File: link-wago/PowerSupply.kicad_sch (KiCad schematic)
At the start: 8 parts, among them U501 TPSM33625

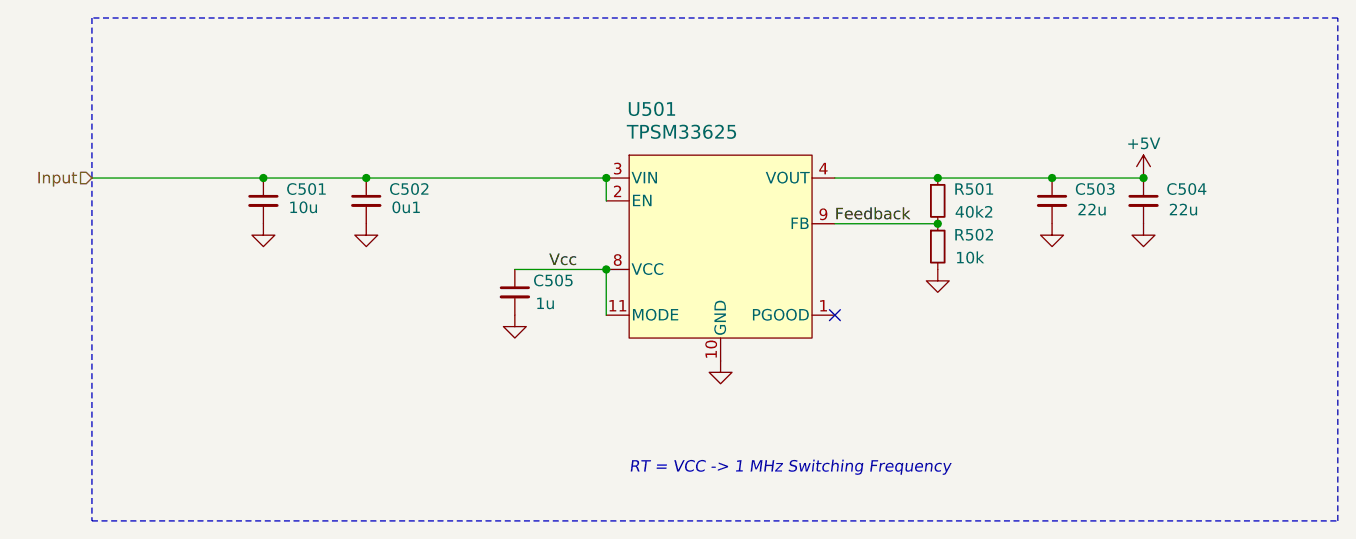
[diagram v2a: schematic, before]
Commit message: Replace step-down
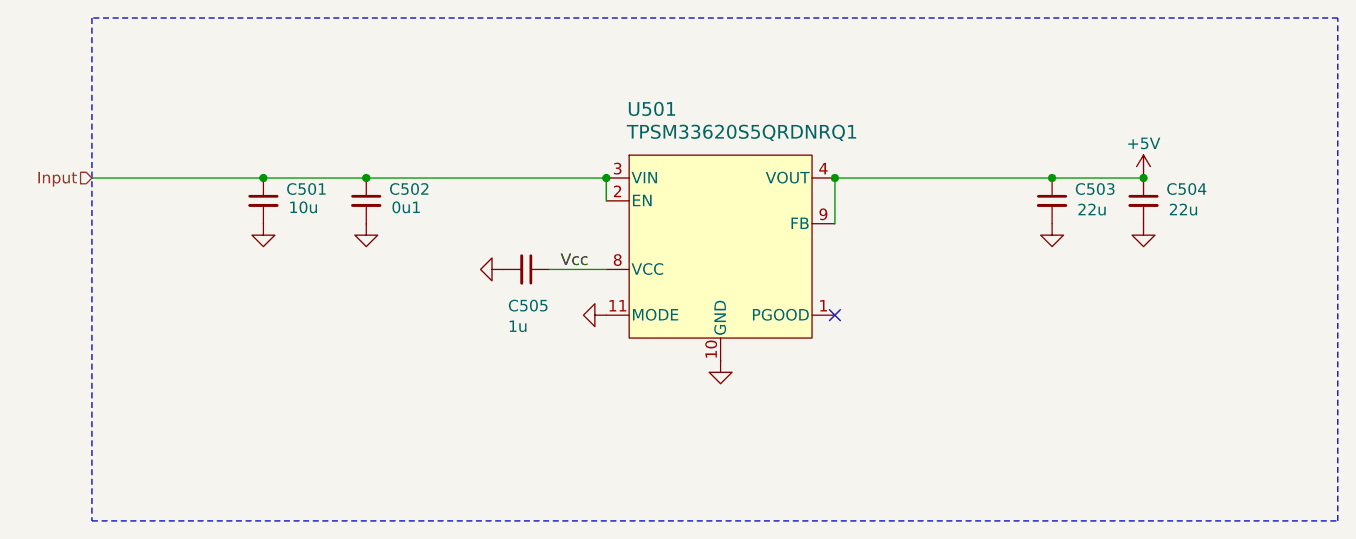
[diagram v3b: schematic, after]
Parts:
- removed R501: 40k2, V2_Resistor_SMD:R_0603, symbol V2_Resistor:0603_40k2
- removed R502: 10k, V2_Resistor_SMD:R_0603, symbol V2_Resistor:0603_10k
- U501: value TPSM33625 -> TPSM33620S5QRDNRQ1; symbol V2_Converter_DCDC:TPSM33625RDNR -> V2_Converter_DCDC:TPSM33620S5QRDNRQ1; Mouser 595-TPSM33625RDNR -> 595-SM33620S5QRDNRQ1; Product TPSM33625RDNR -> TPSM33620S5QRDNRQ1; Rating 2.5A -> 2A
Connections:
- net Feedback is gone; now on net +5V: U501.9 (FB)
- net GND: now also U501.11 (MODE)
- net Vcc: no longer U501.11 (MODE)
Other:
- note removed: "RT = VCC -> 1 MHz Switching Frequency"
- title: Power Supply -> V2 Link WAGO
- moved on the sheet: C505

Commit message: Update
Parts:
- C501: Id (none) -> Capacitor:${SYMBOL_NAME}; Mouser 810-CNA6P1X7R1H106K2 -> 810-CNC6P1X7R1H106K2; Product CNA6P1X7R1H106K250AE -> CNC6P1X7R1H106K250AE
- C502: Id (none) -> Capacitor:${SYMBOL_NAME}
- C503: renamed from C505; Id (none) -> Capacitor:${SYMBOL_NAME}
- C504: renamed from C503; Id (none) -> Capacitor:${SYMBOL_NAME}
- C505: renamed from C504; Id (none) -> Capacitor:${SYMBOL_NAME}
- U501: Id (none) -> DCDC:${SYMBOL_NAME}
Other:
- company: +5V -> Versio Duo
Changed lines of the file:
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@@
 	(title_block
 		(title "V2 Link WAGO")
-		(date "2026-03-31")
+		(date "2026-04-14")
 		(rev "2026-03-31")
-		(company "+5V")
+		(company "Versio Duo")
+		(comment 1 "External Power Supply")
 	)
 	(junction
@@
 			)
 		)
+		(property "Id" "DCDC:${SYMBOL_NAME}"
+			(at 148.59 147.32 0)
+			(hide yes)
+			(show_name no)
+			(do_not_autoplace no)
+			(effects
+				(font
+					(size 1.27 1.27)
+				)
+			)
+		)
 		(pin "1"
 		)
@@
 			)
 		)
+		(property "Id" "Capacitor:${SYMBOL_NAME}"
+			(at 109.22 113.03 0)
+			(hide yes)
+			(show_name no)
+			(do_not_autoplace no)
+			(effects
+				(font
+					(size 1.27 1.27)
+				)
+			)
+		)
 		(pin "1"
 		)
@@
 		(in_pos_files yes)
 		(dnp no)
-		(property "Reference" "C504"
+		(property "Reference" "C505"
 			(at 198.12 96.52 0)
 			(show_name no)
@@
 		(property "Rating" "25V"
 			(at 195.58 118.11 0)
+			(hide yes)
+			(show_name no)
+			(do_not_autoplace no)
+			(effects
+				(font
+					(size 1.27 1.27)
+				)
+			)
+		)
+		(property "Id" "Capacitor:${SYMBOL_NAME}"
+			(at 195.58 113.03 0)
 			(hide yes)
 			(show_name no)
@@
 			(project "link-wago"
 				(path "/6c8448b4-b04d-47e1-934e-e40cbe27a7be/24a9dc0c-cb3c-464a-a734-f09bf949d71a"
-					(reference "C504")
+					(reference "C505")
 					(unit 1)
 				)
@@
 		(in_pos_files yes)
 		(dnp no)
-		(property "Reference" "#PWR504"
+		(property "Reference" "#PWR506"
 			(at 185.42 106.68 0)
 			(hide yes)
@@
 			(project "link-wago"
 				(path "/6c8448b4-b04d-47e1-934e-e40cbe27a7be/24a9dc0c-cb3c-464a-a734-f09bf949d71a"
-					(reference "#PWR504")
+					(reference "#PWR506")
 					(unit 1)
 				)
@@
 		(in_pos_files yes)
 		(dnp no)
-		(property "Reference" "#PWR505"
+		(property "Reference" "#PWR508"
 			(at 195.58 106.68 0)
 			(hide yes)
@@
 			(project "link-wago"
 				(path "/6c8448b4-b04d-47e1-934e-e40cbe27a7be/24a9dc0c-cb3c-464a-a734-f09bf949d71a"
-					(reference "#PWR505")
+					(reference "#PWR508")
 					(unit 1)
 				)
@@
 		(in_pos_files yes)
 		(dnp no)
-		(property "Reference" "#PWR501"
+		(property "Reference" "#PWR507"
 			(at 195.58 99.06 0)
 			(hide yes)
@@
 			(project "link-wago"
 				(path "/6c8448b4-b04d-47e1-934e-e40cbe27a7be/24a9dc0c-cb3c-464a-a734-f09bf949d71a"
-					(reference "#PWR501")
+					(reference "#PWR507")
 					(unit 1)
 				)
@@
 		(in_pos_files yes)
 		(dnp no)
-		(property "Reference" "#PWR502"
+		(property "Reference" "#PWR501"
 			(at 97.79 106.68 0)
 			(hide yes)
@@
 			(project "link-wago"
 				(path "/6c8448b4-b04d-47e1-934e-e40cbe27a7be/24a9dc0c-cb3c-464a-a734-f09bf949d71a"
-					(reference "#PWR502")
+					(reference "#PWR501")
 					(unit 1)
 				)
@@
 		(in_pos_files yes)
 		(dnp no)
-		(property "Reference" "#PWR503"
+		(property "Reference" "#PWR502"
 			(at 109.22 106.68 0)
 			(hide yes)
@@
 			(project "link-wago"
 				(path "/6c8448b4-b04d-47e1-934e-e40cbe27a7be/24a9dc0c-cb3c-464a-a734-f09bf949d71a"
-					(reference "#PWR503")
+					(reference "#PWR502")
 					(unit 1)
 				)
@@
 		(in_pos_files yes)
 		(dnp no)
-		(property "Reference" "C505"
+		(property "Reference" "C503"
 			(at 124.968 109.474 90)
 			(show_name no)
@@
 		(property "Rating" "50V"
 			(at 104.14 105.41 0)
+			(hide yes)
+			(show_name no)
+			(do_not_autoplace no)
+			(effects
+				(font
+					(size 1.27 1.27)
+				)
+			)
+		)
+		(property "Id" "Capacitor:${SYMBOL_NAME}"
+			(at 111.76 105.41 0)
 			(hide yes)
 			(show_name no)
@@
 			(project "link-wago"
 				(path "/6c8448b4-b04d-47e1-934e-e40cbe27a7be/24a9dc0c-cb3c-464a-a734-f09bf949d71a"
-					(reference "C505")
+					(reference "C503")
 					(unit 1)
 				)
@@
 		(in_pos_files yes)
 		(dnp no)
-		(property "Reference" "C503"
+		(property "Reference" "C504"
 			(at 187.96 96.52 0)
 			(show_name no)
@@
 		(property "Rating" "25V"
 			(at 185.42 118.11 0)
+			(hide yes)
+			(show_name no)
+			(do_not_autoplace no)
+			(effects
+				(font
+					(size 1.27 1.27)
+				)
+			)
+		)
+		(property "Id" "Capacitor:${SYMBOL_NAME}"
+			(at 185.42 113.03 0)
 			(hide yes)
 			(show_name no)
@@
 			(project "link-wago"
 				(path "/6c8448b4-b04d-47e1-934e-e40cbe27a7be/24a9dc0c-cb3c-464a-a734-f09bf949d71a"
-					(reference "C503")
+					(reference "C504")
 					(unit 1)
 				)
@@
 		(in_pos_files yes)
 		(dnp no)
-		(property "Reference" "#PWR507"
+		(property "Reference" "#PWR503"
 			(at 118.11 105.41 0)
 			(hide yes)
@@
 			(project "link-wago"
 				(path "/6c8448b4-b04d-47e1-934e-e40cbe27a7be/24a9dc0c-cb3c-464a-a734-f09bf949d71a"
-					(reference "#PWR507")
+					(reference "#PWR503")
 					(unit 1)
 				)
@@
 		(in_pos_files yes)
 		(dnp no)
-		(property "Reference" "#PWR508"
+		(property "Reference" "#PWR505"
 			(at 148.59 121.92 0)
 			(hide yes)
@@
 			(project "link-wago"
 				(path "/6c8448b4-b04d-47e1-934e-e40cbe27a7be/24a9dc0c-cb3c-464a-a734-f09bf949d71a"
-					(reference "#PWR508")
+					(reference "#PWR505")
 					(unit 1)
 				)
@@
 			)
 		)
-		(property "Mouser" "810-CNA6P1X7R1H106K2"
+		(property "Mouser" "810-CNC6P1X7R1H106K2"
 			(at 97.79 114.3 0)
 			(hide yes)
@@
 			)
 		)
-		(property "Product" "CNA6P1X7R1H106K250AE"
+		(property "Product" "CNC6P1X7R1H106K250AE"
 			(at 97.79 115.57 0)
 			(hide yes)
@@
 		(property "Rating" "50V"
 			(at 97.79 118.11 0)
+			(hide yes)
+			(show_name no)
+			(do_not_autoplace no)
+			(effects
+				(font
+					(size 1.27 1.27)
+				)
+			)
+		)
+		(property "Id" "Capacitor:${SYMBOL_NAME}"
+			(at 97.79 113.03 0)
 			(hide yes)
 			(show_name no)
@@
 		(in_pos_files yes)
 		(dnp no)
-		(property "Reference" "#PWR509"
+		(property "Reference" "#PWR504"
 			(at 129.54 110.49 0)
 			(hide yes)
@@
 			(project "link-wago"
 				(path "/6c8448b4-b04d-47e1-934e-e40cbe27a7be/24a9dc0c-cb3c-464a-a734-f09bf949d71a"
-					(reference "#PWR509")
+					(reference "#PWR504")
 					(unit 1)
 				)

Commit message: Good Bye Imperial
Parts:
- C501: footprint V2_Capacitor_SMD:C_1210 -> V2_Capacitor_SMD:C_3225; symbol V2_Capacitor:1210_10u -> V2_Capacitor:3225_10u
- C502: footprint V2_Capacitor_SMD:C_0603 -> V2_Capacitor_SMD:C_1608; symbol V2_Capacitor:0603_0u1 -> V2_Capacitor:1608_0u1
- C503: footprint V2_Capacitor_SMD:C_0603 -> V2_Capacitor_SMD:C_1608; symbol V2_Capacitor:0603_1u -> V2_Capacitor:1608_1u
- C504, C505: footprint V2_Capacitor_SMD:C_1210 -> V2_Capacitor_SMD:C_3225; symbol V2_Capacitor:1210_22u -> V2_Capacitor:3225_22u
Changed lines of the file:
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@@
 	)
 	(symbol
-		(lib_id "V2_Capacitor:0603_0u1")
+		(lib_id "V2_Capacitor:1608_0u1")
 		(at 109.22 97.79 0)
 		(unit 1)
@@
 			)
 		)
-		(property "Footprint" "V2_Capacitor_SMD:C_0603"
+		(property "Footprint" "V2_Capacitor_SMD:C_1608"
 			(at 109.22 114.808 0)
 			(hide yes)
@@
 	)
 	(symbol
-		(lib_id "V2_Capacitor:1210_22u")
+		(lib_id "V2_Capacitor:3225_22u")
 		(at 195.58 97.79 0)
 		(unit 1)
@@
 			)
 		)
-		(property "Footprint" "V2_Capacitor_SMD:C_1210"
+		(property "Footprint" "V2_Capacitor_SMD:C_3225"
 			(at 195.58 114.808 0)
 			(hide yes)
@@
 	)
 	(symbol
-		(lib_id "V2_Capacitor:0603_1u")
+		(lib_id "V2_Capacitor:1608_1u")
 		(at 127 105.41 270)
 		(unit 1)
@@
 			)
 		)
-		(property "Footprint" "V2_Capacitor_SMD:C_0603"
+		(property "Footprint" "V2_Capacitor_SMD:C_1608"
 			(at 109.982 105.41 0)
 			(hide yes)
@@
 	)
 	(symbol
-		(lib_id "V2_Capacitor:1210_22u")
+		(lib_id "V2_Capacitor:3225_22u")
 		(at 185.42 97.79 0)
 		(unit 1)
@@
 			)
 		)
-		(property "Footprint" "V2_Capacitor_SMD:C_1210"
+		(property "Footprint" "V2_Capacitor_SMD:C_3225"
 			(at 185.42 114.808 0)
 			(hide yes)
@@
 	)
 	(symbol
-		(lib_id "V2_Capacitor:1210_10u")
+		(lib_id "V2_Capacitor:3225_10u")
 		(at 97.79 97.79 0)
 		(unit 1)
@@
 			)
 		)
-		(property "Footprint" "V2_Capacitor_SMD:C_1210"
+		(property "Footprint" "V2_Capacitor_SMD:C_3225"
 			(at 97.79 114.808 0)
 			(hide yes)
